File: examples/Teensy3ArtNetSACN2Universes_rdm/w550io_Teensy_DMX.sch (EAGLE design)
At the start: 33 parts, among them IC1 MAX481CPA, IC2 MAX481CPA

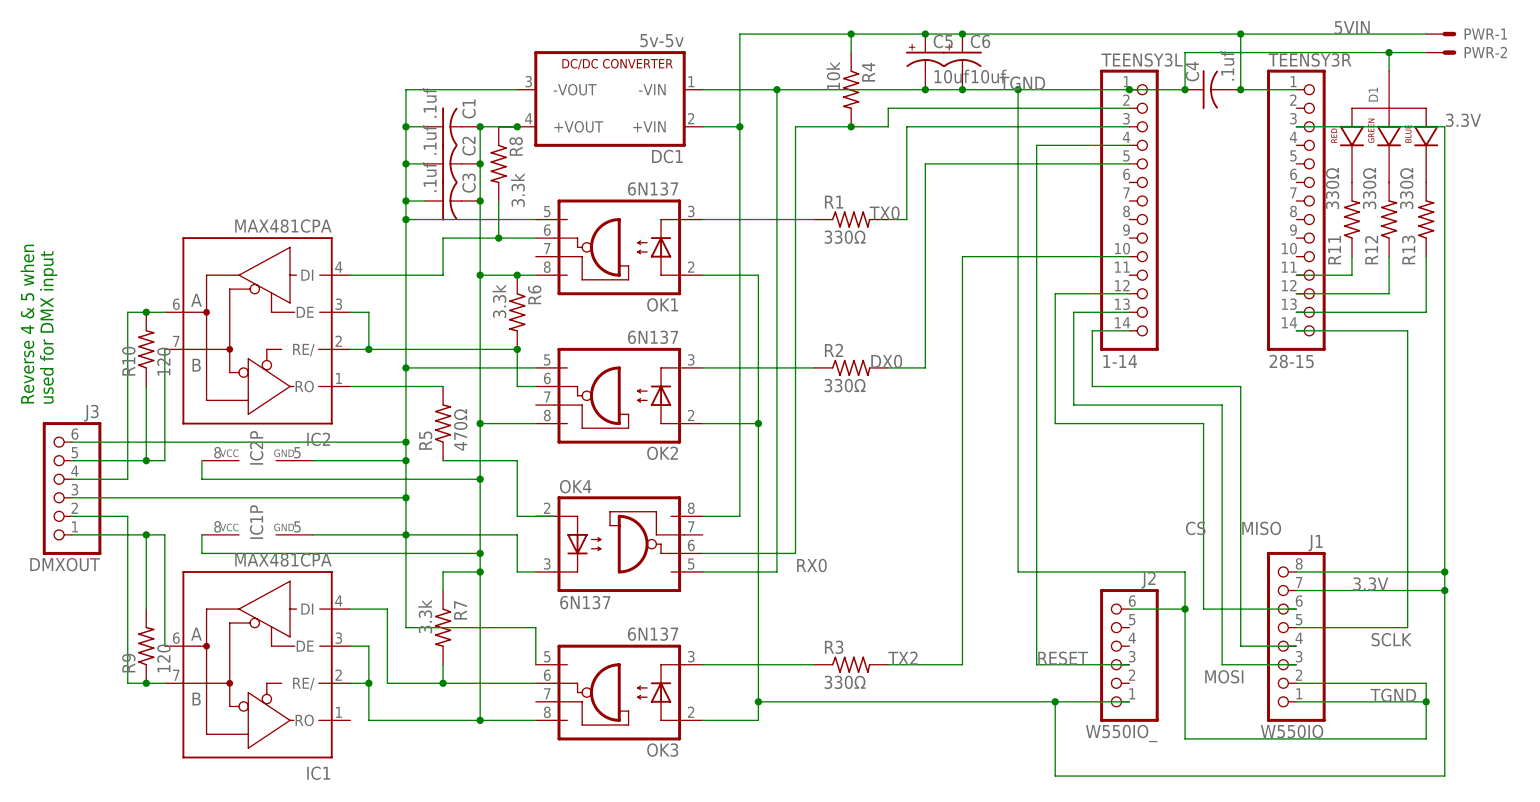
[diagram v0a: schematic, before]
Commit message: Update RDM code and example
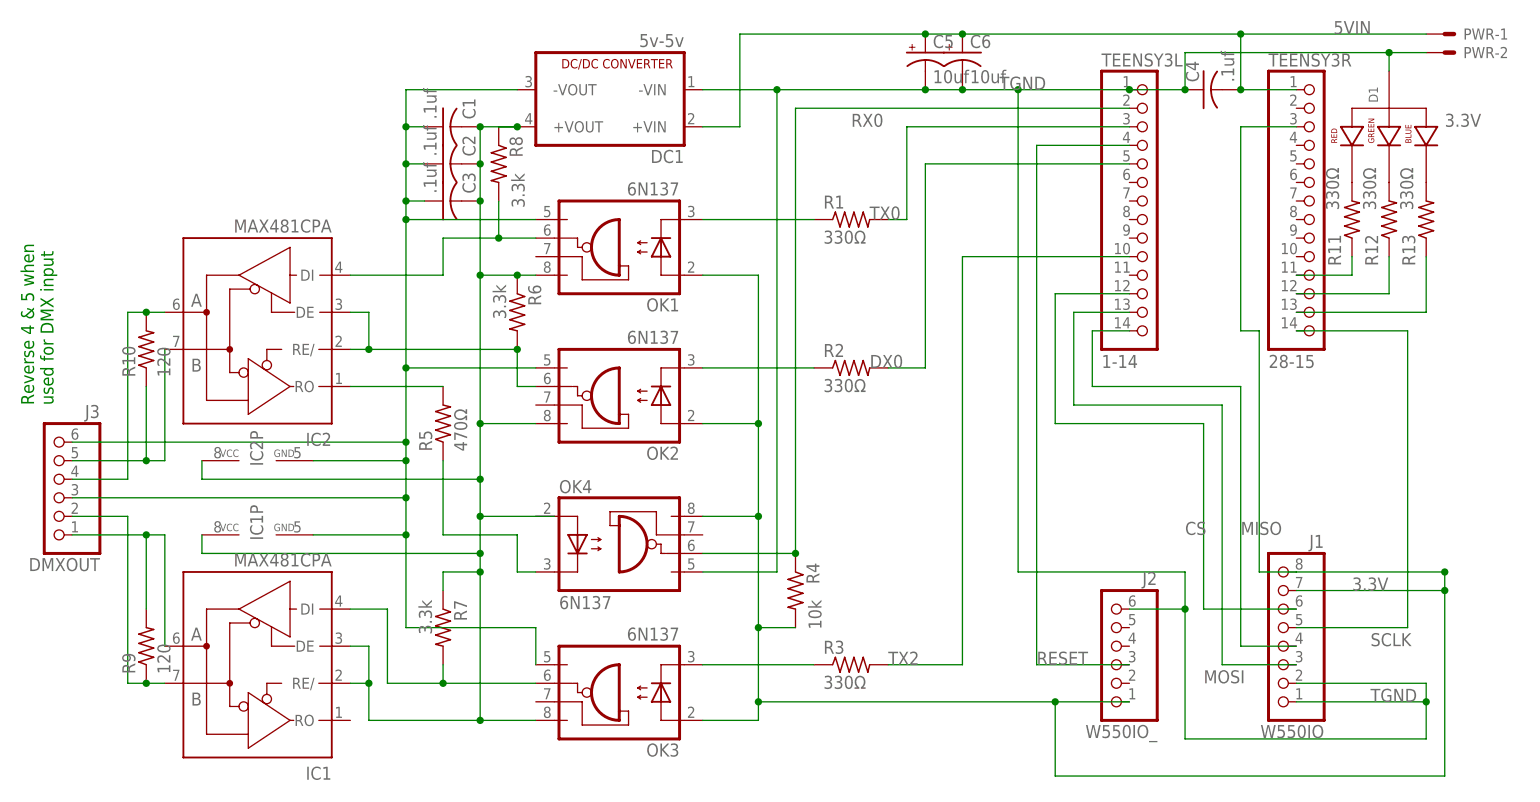
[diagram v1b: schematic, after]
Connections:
- net 3.3V: now also OK4.VCC, R4.2
- net 5VIN: no longer OK4.VCC, R4.1
- net GND: no longer OK4.C
- net N$1: now also OK4.C; no longer OK4.A
- net RX0: now also R4.1; no longer R4.2
- net VCC: now also OK4.A
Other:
- moved on the sheet: R4
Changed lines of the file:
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@@
 <part name="R2" library="adafruit" deviceset="R-US_" device="0204/5" value="330Ω"/>
 <part name="R3" library="adafruit" deviceset="R-US_" device="0204/5" value="330Ω"/>
-<part name="R4" library="adafruit" deviceset="R-US_" device="0204/5" value="10k"/>
 <part name="IC1" library="maxim" deviceset="MAX481CPA" device=""/>
 <part name="IC2" library="maxim" deviceset="MAX481CPA" device=""/>
@@
 <part name="C5" library="adafruit" deviceset="CPOL-US" device="B45181B" value="10uf"/>
 <part name="C6" library="adafruit" deviceset="CPOL-US" device="B45181B" value="10uf"/>
+<part name="R4" library="adafruit" deviceset="R-US_" device="0204/5" value="10k"/>
 </parts>
 <sheets>
@@
 <instance part="R2" gate="G$1" x="93.98" y="45.72"/>
 <instance part="R3" gate="G$1" x="93.98" y="5.08"/>
-<instance part="R4" gate="G$1" x="93.98" y="83.82" rot="R270"/>
 <instance part="IC1" gate="G$1" x="12.7" y="5.08" rot="R180"/>
 <instance part="IC2" gate="G$1" x="12.7" y="50.8" rot="R180"/>
@@
 <instance part="C5" gate="G$1" x="104.14" y="88.9"/>
 <instance part="C6" gate="G$1" x="109.22" y="88.9"/>
+<instance part="R4" gate="G$1" x="86.36" y="15.24" smashed="yes" rot="R270">
+<attribute name="NAME" x="87.8586" y="19.05" size="1.778" layer="95" rot="R270"/>
+<attribute name="VALUE" x="88.138" y="13.97" size="1.778" layer="96" rot="R270"/>
+</instance>
 </instances>
 <busses>
@@
 <segment>
 <pinref part="TEENSY3R" gate="A" pin="3"/>
-<wire x1="154.94" y1="78.74" x2="175.26" y2="78.74" width="0.1524" layer="91"/>
-<wire x1="175.26" y1="78.74" x2="175.26" y2="17.78" width="0.1524" layer="91"/>
+<wire x1="154.94" y1="78.74" x2="147.32" y2="78.74" width="0.1524" layer="91"/>
+<wire x1="147.32" y1="78.74" x2="147.32" y2="50.8" width="0.1524" layer="91"/>
+<wire x1="147.32" y1="50.8" x2="149.86" y2="50.8" width="0.1524" layer="91"/>
+<wire x1="149.86" y1="50.8" x2="149.86" y2="17.78" width="0.1524" layer="91"/>
+<wire x1="149.86" y1="17.78" x2="154.94" y2="17.78" width="0.1524" layer="91"/>
 <wire x1="175.26" y1="17.78" x2="175.26" y2="15.24" width="0.1524" layer="91"/>
 <wire x1="175.26" y1="15.24" x2="175.26" y2="-10.16" width="0.1524" layer="91"/>
@@
 <wire x1="81.28" y1="38.1" x2="73.66" y2="38.1" width="0.1524" layer="91"/>
 <junction x="81.28" y="38.1"/>
-<wire x1="81.28" y1="38.1" x2="81.28" y2="0" width="0.1524" layer="91"/>
+<wire x1="81.28" y1="38.1" x2="81.28" y2="25.4" width="0.1524" layer="91"/>
+<wire x1="81.28" y1="25.4" x2="81.28" y2="10.16" width="0.1524" layer="91"/>
+<wire x1="81.28" y1="10.16" x2="81.28" y2="0" width="0.1524" layer="91"/>
 <wire x1="81.28" y1="-2.54" x2="73.66" y2="-2.54" width="0.1524" layer="91"/>
 <wire x1="121.92" y1="0" x2="81.28" y2="0" width="0.1524" layer="91"/>
@@
 <junction x="81.28" y="0"/>
 <junction x="121.92" y="0"/>
+<pinref part="OK4" gate="A" pin="VCC"/>
+<wire x1="73.66" y1="25.4" x2="81.28" y2="25.4" width="0.1524" layer="91"/>
+<junction x="81.28" y="25.4"/>
+<pinref part="R4" gate="G$1" pin="2"/>
+<wire x1="86.36" y1="10.16" x2="81.28" y2="10.16" width="0.1524" layer="91"/>
+<junction x="81.28" y="10.16"/>
 </segment>
 </net>
@@
 <pinref part="TEENSY3R" gate="A" pin="1"/>
 <wire x1="147.32" y1="83.82" x2="154.94" y2="83.82" width="0.1524" layer="91"/>
-<pinref part="R4" gate="G$1" pin="1"/>
-<wire x1="93.98" y1="88.9" x2="93.98" y2="91.44" width="0.1524" layer="91"/>
-<wire x1="78.74" y1="91.44" x2="93.98" y2="91.44" width="0.1524" layer="91"/>
-<wire x1="93.98" y1="91.44" x2="104.14" y2="91.44" width="0.1524" layer="91"/>
-<junction x="93.98" y="91.44"/>
+<wire x1="78.74" y1="91.44" x2="104.14" y2="91.44" width="0.1524" layer="91"/>
 <pinref part="PWR" gate="-1" pin="S"/>
 <wire x1="104.14" y1="91.44" x2="109.22" y2="91.44" width="0.1524" layer="91"/>
@@
 <pinref part="C6" gate="G$1" pin="+"/>
 <junction x="109.22" y="91.44"/>
-<wire x1="78.74" y1="25.4" x2="78.74" y2="78.74" width="0.1524" layer="91"/>
-<junction x="78.74" y="78.74"/>
-<pinref part="OK4" gate="A" pin="VCC"/>
-<wire x1="78.74" y1="25.4" x2="73.66" y2="25.4" width="0.1524" layer="91"/>
 </segment>
 </net>
@@
 <wire x1="50.8" y1="5.08" x2="50.8" y2="10.16" width="0.1524" layer="91"/>
 <wire x1="50.8" y1="10.16" x2="33.02" y2="10.16" width="0.1524" layer="91"/>
-<wire x1="33.02" y1="22.86" x2="48.26" y2="22.86" width="0.1524" layer="91"/>
-<pinref part="OK4" gate="A" pin="C"/>
-<wire x1="50.8" y1="17.78" x2="48.26" y2="17.78" width="0.1524" layer="91"/>
-<wire x1="48.26" y1="22.86" x2="48.26" y2="17.78" width="0.1524" layer="91"/>
 </segment>
 </net>
@@
 <junction x="43.18" y="58.42"/>
 <wire x1="43.18" y1="38.1" x2="43.18" y2="30.48" width="0.1524" layer="91"/>
-<wire x1="43.18" y1="30.48" x2="43.18" y2="20.32" width="0.1524" layer="91"/>
+<wire x1="43.18" y1="30.48" x2="43.18" y2="25.4" width="0.1524" layer="91"/>
+<wire x1="43.18" y1="25.4" x2="43.18" y2="20.32" width="0.1524" layer="91"/>
 <wire x1="43.18" y1="20.32" x2="43.18" y2="17.78" width="0.1524" layer="91"/>
 <wire x1="43.18" y1="17.78" x2="43.18" y2="-2.54" width="0.1524" layer="91"/>
@@
 <wire x1="27.94" y1="7.62" x2="25.4" y2="7.62" width="0.1524" layer="91"/>
 <junction x="27.94" y="2.54"/>
+<pinref part="OK4" gate="A" pin="A"/>
+<wire x1="43.18" y1="25.4" x2="50.8" y2="25.4" width="0.1524" layer="91"/>
+<wire x1="50.8" y1="25.4" x2="53.34" y2="25.4" width="0.1524" layer="91"/>
+<junction x="43.18" y="25.4"/>
 </segment>
 </net>
 <net name="RX0" class="0">
 <segment>
+<label x="93.98" y="78.74" size="1.778" layer="95"/>
 <pinref part="TEENSY3L" gate="A" pin="2"/>
-<wire x1="86.36" y1="20.32" x2="86.36" y2="78.74" width="0.1524" layer="91"/>
-<label x="86.36" y="17.78" size="1.778" layer="95"/>
+<wire x1="86.36" y1="81.28" x2="132.08" y2="81.28" width="0.1524" layer="91"/>
 <pinref part="OK4" gate="A" pin="VO"/>
-<wire x1="99.06" y1="81.28" x2="132.08" y2="81.28" width="0.1524" layer="91"/>
 <wire x1="86.36" y1="20.32" x2="73.66" y2="20.32" width="0.1524" layer="91"/>
-<wire x1="99.06" y1="81.28" x2="99.06" y2="78.74" width="0.1524" layer="91"/>
-<wire x1="99.06" y1="78.74" x2="93.98" y2="78.74" width="0.1524" layer="91"/>
-<pinref part="R4" gate="G$1" pin="2"/>
-<wire x1="93.98" y1="78.74" x2="86.36" y2="78.74" width="0.1524" layer="91"/>
-<junction x="93.98" y="78.74"/>
+<wire x1="86.36" y1="20.32" x2="86.36" y2="81.28" width="0.1524" layer="91"/>
+<pinref part="R4" gate="G$1" pin="1"/>
+<junction x="86.36" y="20.32"/>
 </segment>
 </net>
@@
 <net name="N$1" class="0">
 <segment>
+<pinref part="OK4" gate="A" pin="C"/>
+<wire x1="50.8" y1="17.78" x2="48.26" y2="17.78" width="0.1524" layer="91"/>
+<wire x1="48.26" y1="22.86" x2="48.26" y2="17.78" width="0.1524" layer="91"/>
+<wire x1="48.26" y1="22.86" x2="38.1" y2="22.86" width="0.1524" layer="91"/>
 <pinref part="R5" gate="G$1" pin="1"/>
-<wire x1="48.26" y1="33.02" x2="38.1" y2="33.02" width="0.1524" layer="91"/>
-<wire x1="48.26" y1="33.02" x2="48.26" y2="25.4" width="0.1524" layer="91"/>
-<pinref part="OK4" gate="A" pin="A"/>
-<wire x1="48.26" y1="25.4" x2="50.8" y2="25.4" width="0.1524" layer="91"/>
-<wire x1="50.8" y1="25.4" x2="53.34" y2="25.4" width="0.1524" layer="91"/>
-</segment>
-</net>
+<wire x1="38.1" y1="22.86" x2="38.1" y2="33.02" width="0.1524" layer="91"/>
+</segment>
+</net>
